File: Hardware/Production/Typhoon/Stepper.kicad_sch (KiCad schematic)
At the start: 11 parts, among them IC1 TMC2209-LA, J3 Motor Breakout

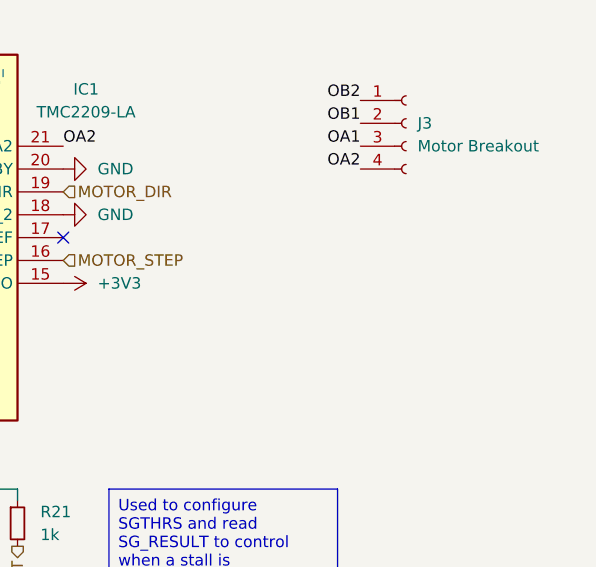
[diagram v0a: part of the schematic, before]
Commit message: Added in power socket onto stepper.sch somehow i forgot it lol
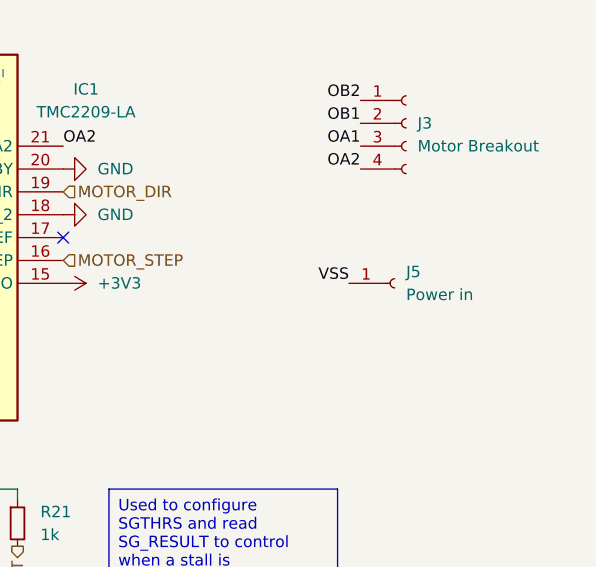
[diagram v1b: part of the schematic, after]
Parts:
- added J5: Power in, symbol Connector:Conn_01x01_Socket
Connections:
- net VSS: now also J5.1 (Pin_1)
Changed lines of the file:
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@@
+		)
+	)
+	(label "VSS"
+		(at 171.45 113.03 180)
+		(fields_autoplaced yes)
+		(effects
+			(font
+				(size 1.27 1.27)
+			)
+			(justify right bottom)
 		)
 	)
@@
 					(unit 1)
 				)
+			)
+		)
+	)
+	(symbol
+		(lib_id "Connector:Conn_01x01_Socket")
+		(at 176.53 113.03 0)
+		(unit 1)
+		(exclude_from_sim no)
+		(in_bom yes)
+		(on_board yes)
+		(dnp no)
+		(fields_autoplaced yes)
+		(property "Reference" "J5"
+			(at 177.8 111.7599 0)
+			(effects
+				(font
+					(size 1.27 1.27)
+				)
+				(justify left)
+			)
+		)
+		(property "Value" "Power in"
+			(at 177.8 114.2999 0)
+			(effects
+				(font
+					(size 1.27 1.27)
+				)
+				(justify left)
+			)
+		)
+		(property "Footprint" ""
+			(at 176.53 113.03 0)
+			(effects
+				(font
+					(size 1.27 1.27)
+				)
+				(hide yes)
+			)
+		)
+		(property "Datasheet" "~"
+			(at 176.53 113.03 0)
+			(effects
+				(font
+					(size 1.27 1.27)
+				)
+				(hide yes)
+			)
+		)
+		(property "Description" "Generic connector, single row, 01x01, script generated"
+			(at 176.53 113.03 0)
+			(effects
+				(font
+					(size 1.27 1.27)
+				)
+				(hide yes)
+			)
+		)
+		(pin "1"
+		)
+		(instances
+			(project ""
+				(path "/7db990e4-92e1-4f99-b4d2-435bbec1ba83/8de86a23-669c-43a7-bbab-df851b7a13ef"
+					(reference "J5")
+					(unit 1)
+				)

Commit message: Finished footprinting and started the PCB layout
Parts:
- C12, C18, C19, C28, C29: footprint (none) -> Capacitor_SMD:C_0402_1005Metric
- C30: footprint (none) -> Capacitor_Tantalum_SMD:CP_EIA-7360-38_Kemet-E
- J3: footprint (none) -> Connector_PinSocket_2.54mm:PinSocket_1x04_P2.54mm_Horizontal
- J5: footprint (none) -> Connector_PinSocket_2.54mm:PinSocket_1x01_P2.54mm_Horizontal
- R19, R20, R21: footprint (none) -> Resistor_SMD:R_0402_1005Metric
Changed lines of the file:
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@@
 			)
 		)
-		(property "Footprint" ""
+		(property "Footprint" "Capacitor_SMD:C_0402_1005Metric"
 			(at 100.33 63.5 0)
 			(effects
@@
 			)
 		)
-		(property "Footprint" ""
+		(property "Footprint" "Capacitor_SMD:C_0402_1005Metric"
 			(at 132.08 60.96 0)
 			(effects
@@
 			)
 		)
-		(property "Footprint" ""
+		(property "Footprint" "Capacitor_SMD:C_0402_1005Metric"
 			(at 116.84 60.96 0)
 			(effects
@@
 			)
 		)
-		(property "Footprint" ""
+		(property "Footprint" "Resistor_SMD:R_0402_1005Metric"
 			(at 134.62 139.7 0)
 			(effects
@@
 			)
 		)
-		(property "Footprint" ""
+		(property "Footprint" "Capacitor_SMD:C_0402_1005Metric"
 			(at 114.3 135.89 0)
 			(effects
@@
 			)
 		)
-		(property "Footprint" ""
+		(property "Footprint" "Resistor_SMD:R_0402_1005Metric"
 			(at 119.38 74.93 0)
 			(effects
@@
 			)
 		)
-		(property "Footprint" ""
+		(property "Footprint" "Connector_PinSocket_2.54mm:PinSocket_1x01_P2.54mm_Horizontal"
 			(at 176.53 113.03 0)
 			(effects
@@
 			)
 		)
-		(property "Footprint" ""
+		(property "Footprint" "Capacitor_Tantalum_SMD:CP_EIA-7360-38_Kemet-E"
 			(at 144.78 60.96 0)
 			(effects
@@
 			)
 		)
-		(property "Footprint" ""
+		(property "Footprint" "Resistor_SMD:R_0402_1005Metric"
 			(at 129.54 74.93 0)
 			(effects
@@
 			)
 		)
-		(property "Footprint" ""
+		(property "Footprint" "Connector_PinSocket_2.54mm:PinSocket_1x04_P2.54mm_Horizontal"
 			(at 177.8 95.25 0)
 			(effects
@@
 			)
 		)
-		(property "Footprint" ""
+		(property "Footprint" "Capacitor_SMD:C_0402_1005Metric"
 			(at 101.6 107.95 0)
 			(effects

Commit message: Slight updates to the schematic and more PCB layout
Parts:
- removed J5: Power in, Connector_PinSocket_2.54mm:PinSocket_1x01_P2.54mm_Horizontal, symbol Connector:Conn_01x01_Socket
- J3: footprint Connector_PinSocket_2.54mm:PinSocket_1x04_P2.54mm_Horizontal -> Connector_Molex:Molex_Nano-Fit_105313-xx04_1x04_P2.50mm_Horizontal
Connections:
- net VSS renamed +16.8V

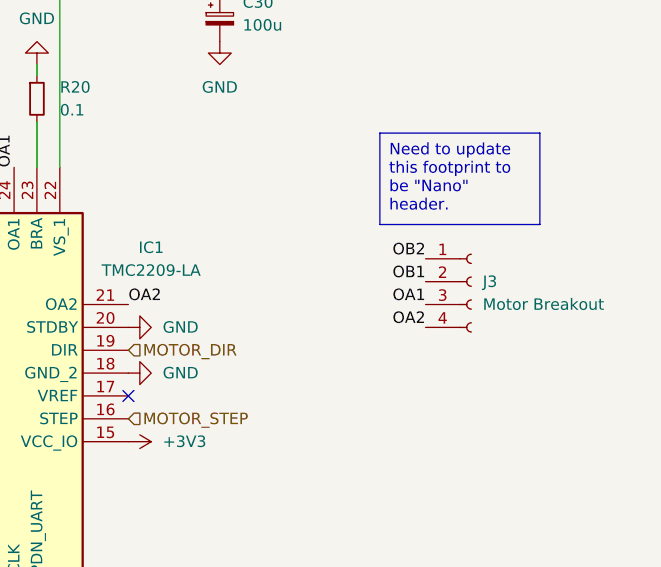
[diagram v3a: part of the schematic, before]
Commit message: Rough Board Layout (Need Review)
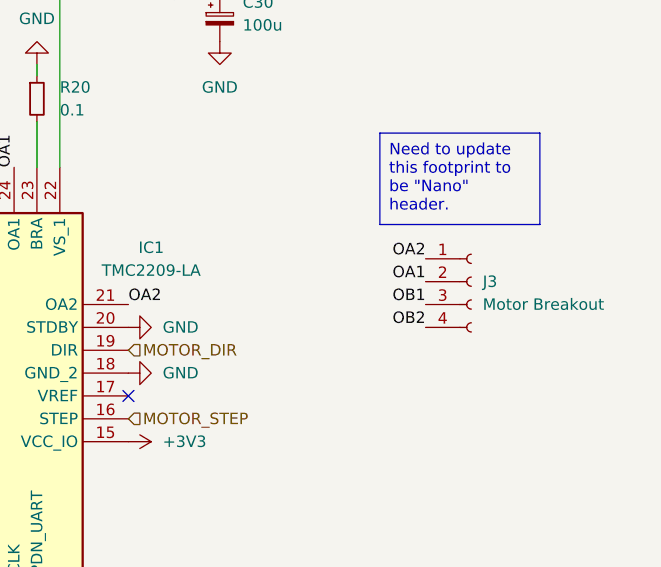
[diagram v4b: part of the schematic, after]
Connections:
- net OA1: now also J3.2 (Pin_2); no longer J3.3 (Pin_3)
- net OA2: now also J3.1 (Pin_1); no longer J3.4 (Pin_4)
- net OB1: now also J3.3 (Pin_3); no longer J3.2 (Pin_2)
- net OB2: now also J3.4 (Pin_4); no longer J3.1 (Pin_1)
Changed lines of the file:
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@@
 	)
 	(label "OB2"
-		(at 172.72 92.71 180)
+		(at 172.72 100.33 180)
 		(fields_autoplaced yes)
 		(effects
@@
 	)
 	(label "OA2"
-		(at 172.72 100.33 180)
+		(at 172.72 92.71 180)
 		(fields_autoplaced yes)
 		(effects
@@
 	)
 	(label "OA1"
-		(at 172.72 97.79 180)
+		(at 172.72 95.25 180)
 		(fields_autoplaced yes)
 		(effects
@@
 	)
 	(label "OB1"
-		(at 172.72 95.25 180)
+		(at 172.72 97.79 180)
 		(fields_autoplaced yes)
 		(effects
@@
 		(on_board yes)
 		(dnp no)
-		(fields_autoplaced yes)
 		(property "Reference" "J3"
 			(at 179.07 95.2499 0)

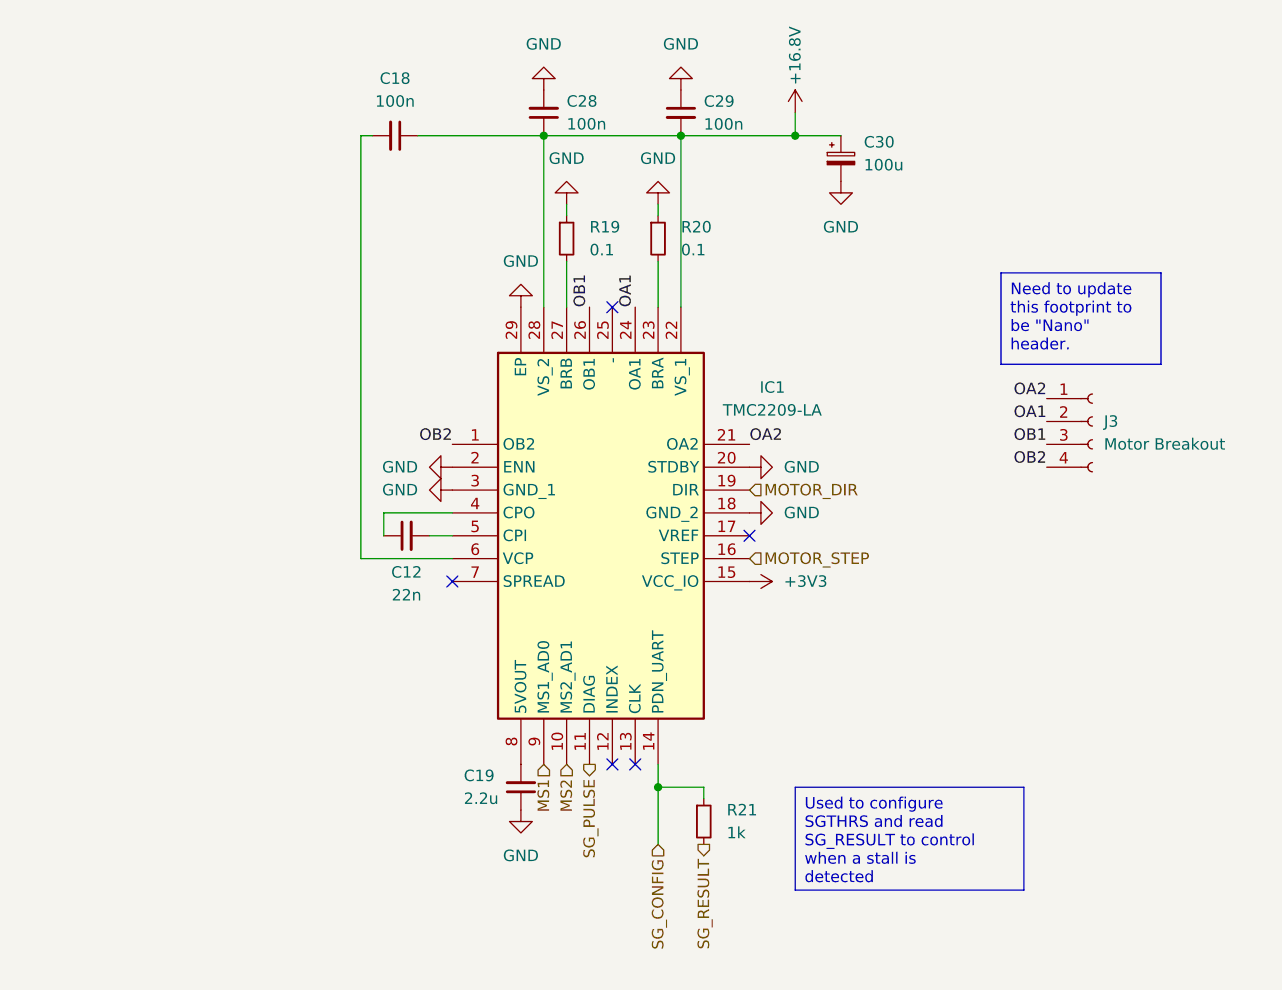
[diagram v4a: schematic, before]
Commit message: Updated schematic, added mosfets to ENN and SPREAD pins of TMC2209 and connected INDEX, CLK, and VREF to GPIO pins
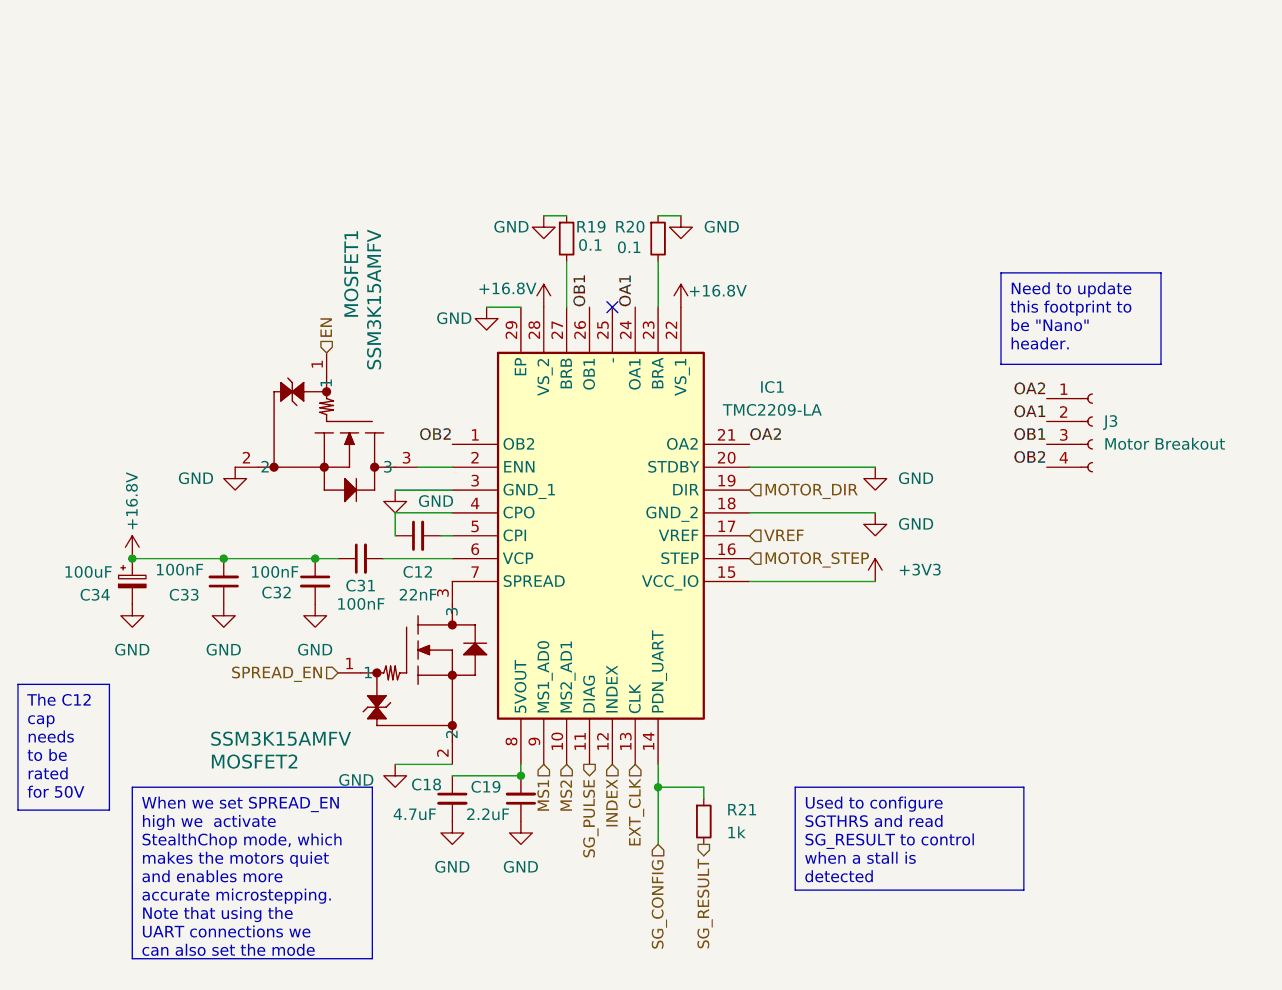
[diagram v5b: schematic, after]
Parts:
- removed C28, C29: 100n, Capacitor_SMD:C_0402_1005Metric, symbol Device:C_Small
- removed C30: 100u, Capacitor_Tantalum_SMD:CP_EIA-7360-38_Kemet-E, symbol Device:C_Polarized_Small
- added C31, C32, C33: 100nF, Capacitor_SMD:C_0402_1005Metric, symbol Device:C_Small
- added C34: 100uF, Capacitor_Tantalum_SMD:CP_EIA-7360-38_Kemet-E, symbol Device:C_Polarized_Small
- added MOSFET1, MOSFET2: SSM3K15AMFV, VESM_TOS, symbol SSM3K15AMFV:SSM3K15AMFV
- C12: value 22n -> 22nF
- C18: value 100n -> 4.7uF
- C19: value 2.2u -> 2.2uF
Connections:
- net +16.8V: now also C31.1, C32.1, C33.2, C34.1; no longer C18.1
- net GND: now also C18.2, C32.2, C33.1, C34.2, MOSFET1.2, MOSFET2.2; no longer IC1.2 (ENN)
- net at IC1.6 (VCP): now also C31.2; no longer C18.2
- net at C19.2, IC1.8 (5VOUT): now also C18.1
- net INDEX: now reaches IC1.12 (INDEX)
- net EXT_CLK: now reaches IC1.13 (CLK)
- net VREF: now reaches IC1.17 (VREF)
- net at IC1.7 (SPREAD): now also MOSFET2.3
- new net: IC1.2 (ENN), MOSFET1.3
- new net EN: MOSFET1.1
- new net SPREAD_EN: MOSFET2.1
- no-connect marks 5 -> 1
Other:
- moved on the sheet: C12, C19
